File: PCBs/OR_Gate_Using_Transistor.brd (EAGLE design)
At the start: 28 x 26.8 mm, 11 parts, among them T1 BC547, T2 BC547

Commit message: Updated
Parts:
- moved OUTPUT 27.3 mm to (19.3, 31.6), turned to 180 degrees
- moved B 20.9 mm to (11.7, 31.6), turned to 180 degrees
- moved A 19.3 mm to (4.28, 31.7), turned to 180 degrees
- moved 5V 7.98 mm to (4.21, 7.09)
- moved GND 7.36 mm to (11.8, 7.05)
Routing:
- net 5V: track 33.3 -> 13.8 mm
- net N$7: track 5.23 -> 20.7 mm
- net N$6: track 6.89 -> 20.3 mm
- net N$3: track 30.9 -> 28.7 mm
- net GND: track 23.0 -> 23.5 mm
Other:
- board size 28 x 26.8 mm -> 29.8 x 38.8 mm
- board text added: "PinwheelRobotics"
- board text added: "care@pinwheel.in"

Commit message: New Update
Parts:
- moved OUTPUT 0.39 mm to (19.2, 32.0)
- moved B 0.38 mm to (11.8, 31.9)
- moved A 0.26 mm to (4.22, 31.9)
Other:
- board size 29.8 x 38.8 mm -> 29.5 x 39.1 mm
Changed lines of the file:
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@@
 <drawing>
 <settings>
-<setting alwaysvectorfont="yes"/>
+<setting alwaysvectorfont="no"/>
 <setting verticaltext="up"/>
 </settings>
@@
 <board>
 <plain>
-<wire x1="-3" y1="0" x2="26.8" y2="-0.061" width="0" layer="20"/>
-<wire x1="26.8" y1="-0.061" x2="26.8" y2="38.726" width="0" layer="20"/>
-<wire x1="26.8" y1="38.726" x2="-2.9" y2="38.66" width="0" layer="20"/>
-<wire x1="-2.9" y1="38.66" x2="-3" y2="0" width="0" layer="20"/>
-<hole x="-1" y="36.5" drill="3"/>
-<hole x="24.5" y="36.5" drill="3"/>
+<wire x1="-3" y1="38.198590625" x2="-3" y2="1.653915625" width="0" layer="20"/>
+<wire x1="-3" y1="1.653915625" x2="-1.3460875" y2="-0.00341875" width="0" layer="20" curve="89.881486"/>
+<wire x1="-1.3460875" y1="-0.00341875" x2="24.954165625" y2="-0.057803125" width="0" layer="20"/>
+<wire x1="24.954165625" y1="-0.057803125" x2="26.5" y2="1.4848375" width="0" layer="20" curve="90.106059"/>
+<wire x1="26.5" y1="1.4848375" x2="26.5" y2="37.990275" width="0" layer="20"/>
+<wire x1="26.5" y1="37.990275" x2="25.490275" y2="39" width="0" layer="20" curve="90"/>
+<wire x1="25.490275" y1="39" x2="-2.198590625" y2="39" width="0" layer="20"/>
+<wire x1="-2.198590625" y1="39" x2="-3" y2="38.198590625" width="0" layer="20" curve="90"/>
+<hole x="-1" y="37" drill="3"/>
+<hole x="24.5" y="37" drill="3"/>
 <hole x="-1" y="2" drill="3"/>
-<hole x="24.5" y="2.5" drill="3"/>
+<hole x="24.5" y="2" drill="3"/>
 <text x="0" y="10.5" size="1.778" layer="21" rot="R90">PinwheelRobotics</text>
-<text x="20" y="25.5" size="1.778" layer="22" rot="MR270">care@pinwheel.in</text>
+<text x="24.572" y="27.786" size="1.778" layer="22" rot="MR270">care@pinwheel.in</text>
 </plain>
 <attributes>
@@
 <attribute name="NAME" x="3.32" y="10.773" size="0.4064" layer="21" font="vector"/>
 </element>
-<element name="A" library="microbit" package="MICROBIT_PAD" value="MICROBIT_PAD" x="4.278" y="31.657" smashed="yes" rot="R180">
-<attribute name="NAME" x="4.913" y="28.101" size="1.27" layer="21" rot="R180"/>
-</element>
-<element name="B" library="microbit" package="MICROBIT_PAD" value="MICROBIT_PAD" x="11.746" y="31.554" smashed="yes" rot="R180">
-<attribute name="NAME" x="13.016" y="27.617" size="0.4064" layer="21" rot="R180"/>
+<element name="A" library="microbit" package="MICROBIT_PAD" value="MICROBIT_PAD" x="4.223" y="31.915" smashed="yes" rot="R180">
+<attribute name="NAME" x="4.858" y="28.359" size="1.27" layer="21" rot="R180"/>
+</element>
+<element name="B" library="microbit" package="MICROBIT_PAD" value="MICROBIT_PAD" x="11.811" y="31.931" smashed="yes" rot="R180">
+<attribute name="NAME" x="13.081" y="27.994" size="0.4064" layer="21" rot="R180"/>
 </element>
 <element name="GND" library="microbit" package="MICROBIT_PAD" value="MICROBIT_PAD" x="11.808" y="7.051" smashed="yes">
@@
 <attribute name="VALUE" x="12.7" y="21.971" size="1.27" layer="27" ratio="10"/>
 </element>
-<element name="OUTPUT" library="microbit" package="MICROBIT_PAD" value="MICROBIT_PAD" x="19.295" y="31.596" smashed="yes" rot="R180">
-<attribute name="NAME" x="15.993" y="28.167" size="0.3048" layer="21" font="vector"/>
+<element name="OUTPUT" library="microbit" package="MICROBIT_PAD" value="MICROBIT_PAD" x="19.226" y="31.981" smashed="yes" rot="R180">
+<attribute name="NAME" x="18.337" y="28.044" size="0.3048" layer="21" font="vector"/>
 </element>
 <element name="R1" library="we-rcl" package="R0207/7" value="" x="10.922" y="15.621" smashed="yes" rot="R180">
@@
 <wire x1="7.5" y1="19.5" x2="7.045" y2="19.05" width="0.254" layer="16"/>
 <wire x1="17.5" y1="31.5" x2="10" y2="24" width="0.254" layer="1"/>
-<wire x1="19" y1="31.5" x2="17.5" y2="31.5" width="0.254" layer="1"/>
+<wire x1="17.747928125" y1="31.5" x2="17.5" y2="31.5" width="0.254" layer="1"/>
 <wire x1="10" y1="24" x2="9.525" y2="23.622" width="0.254" layer="1"/>
-<wire x1="19" y1="31.5" x2="19.295" y2="31.596" width="0.254" layer="1"/>
+<wire x1="17.747928125" y1="31.5" x2="19.226" y2="31.981" width="0.254" layer="1"/>
 </signal>
 <signal name="GND">
@@
 <contactref element="R1" pad="1"/>
 <wire x1="4.5" y1="26" x2="14.5" y2="16" width="0.254" layer="1"/>
-<wire x1="4.5" y1="31.5" x2="4.5" y2="26" width="0.254" layer="1"/>
+<wire x1="4.5" y1="31.719103125" x2="4.5" y2="26" width="0.254" layer="1"/>
 <wire x1="14.5" y1="16" x2="14.672" y2="15.621" width="0.254" layer="1"/>
-<wire x1="4.5" y1="31.5" x2="4.278" y2="31.657" width="0.254" layer="1"/>
+<wire x1="4.5" y1="31.719103125" x2="4.223" y2="31.915" width="0.254" layer="1"/>
 </signal>
 <signal name="N$7">
@@
 <wire x1="13.5" y1="13.5" x2="14.5" y2="12.5" width="0.254" layer="16"/>
 <wire x1="13.5" y1="30" x2="13.5" y2="13.5" width="0.254" layer="16"/>
-<wire x1="12" y1="31.5" x2="13.5" y2="30" width="0.254" layer="16"/>
+<wire x1="11.876340625" y1="31.623659375" x2="13.5" y2="30" width="0.254" layer="16"/>
 <wire x1="14.5" y1="12.5" x2="14.545" y2="12.065" width="0.254" layer="16"/>
-<wire x1="12" y1="31.5" x2="11.746" y2="31.554" width="0.254" layer="16"/>
+<wire x1="11.876340625" y1="31.623659375" x2="11.811" y2="31.931" width="0.254" layer="16"/>
 </signal>
 </signals>

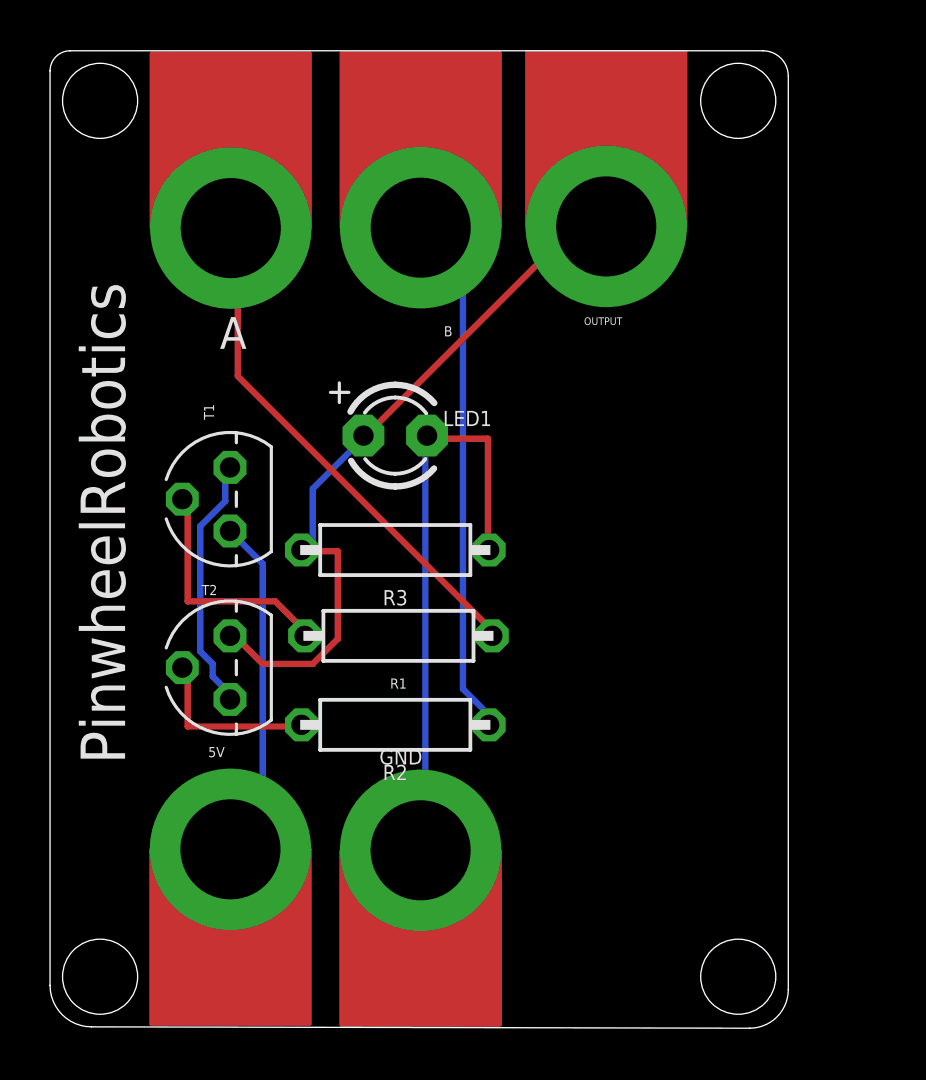
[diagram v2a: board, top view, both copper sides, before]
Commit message: New Update for board curv
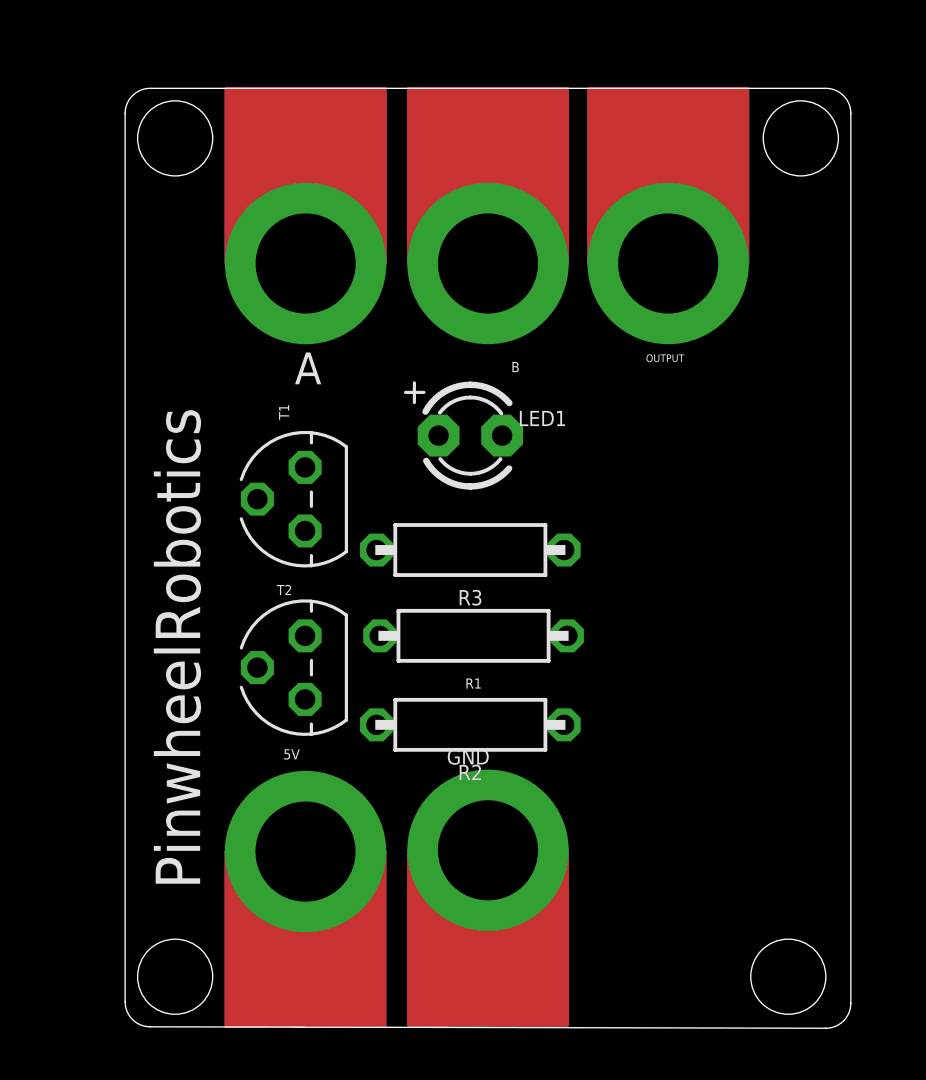
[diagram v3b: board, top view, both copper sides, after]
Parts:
- moved A 3.31 mm to (7.21, 30.5)
- moved B 3.05 mm to (14.5, 30.5)
- moved 5V 3.00 mm to (7.21, 7.00)
- moved LED1 3.00 mm to (13.8, 23.6)
- moved R1 3.00 mm to (13.9, 15.6)
- moved R2 3.00 mm to (13.8, 12.1)
- moved R3 3.00 mm to (13.8, 19.1)
- moved T1 3.00 mm to (7.19, 21.1)
- moved T2 3.00 mm to (7.19, 14.4)
- moved OUTPUT 2.88 mm to (21.7, 30.5)
- moved GND 2.69 mm to (14.5, 7.05)
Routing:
- net N$3: track 28.7 -> 0.00 mm
- net GND: track 23.5 -> 0.00 mm
- net N$7: track 21.0 -> 0.00 mm
- net N$6: track 20.6 -> 0.00 mm
- net 5V: track 13.8 -> 0.00 mm
- net N$2: track 10.2 -> 0.00 mm
- net N$4: track 9.56 -> 0.00 mm
- net N$1: track 6.99 -> 0.00 mm
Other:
- board size 29.5 x 39.1 mm -> 29 x 37.6 mm

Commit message: Dimension added
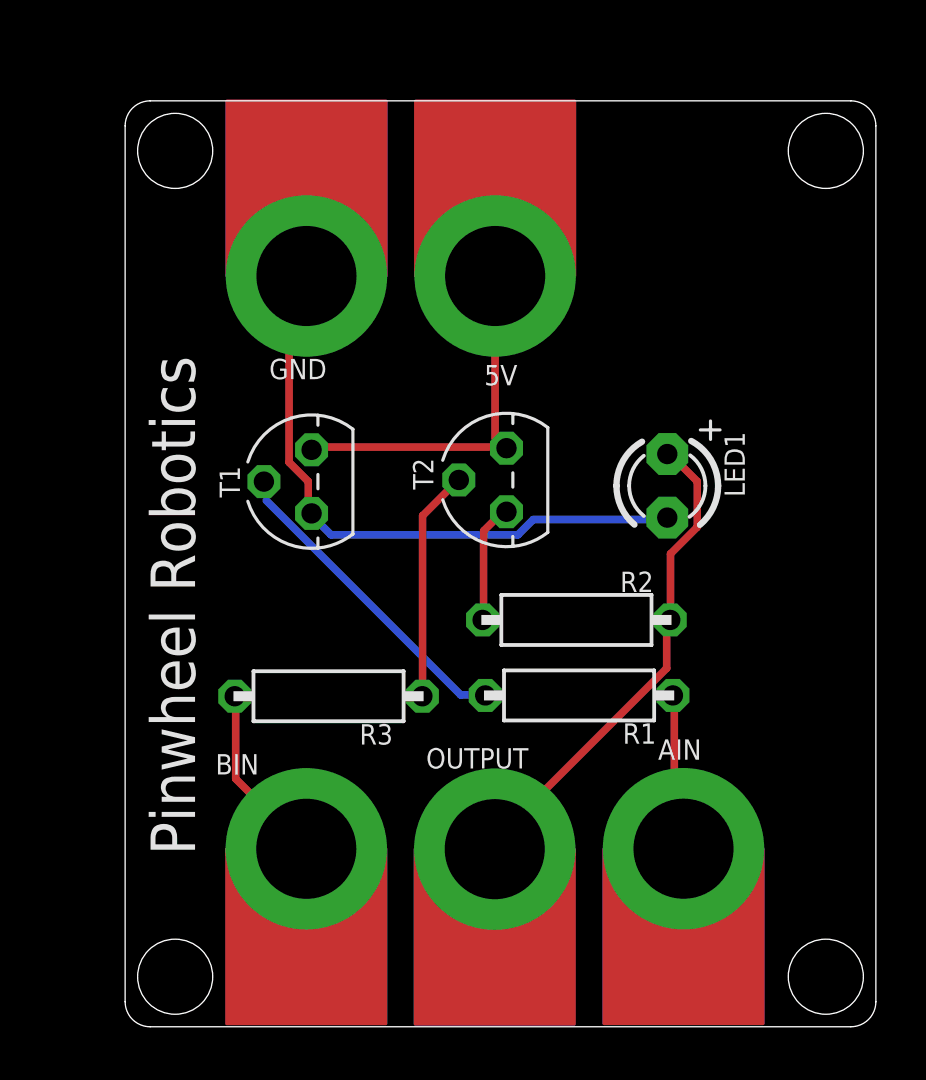
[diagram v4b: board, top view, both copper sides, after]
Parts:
- removed A, B: MICROBIT_PAD, microbit:MICROBIT_PAD
- added AIN, BIN: MICROBIT_PAD, microbit:MICROBIT_PAD
- R1, R3: value (none) -> 10k
- R2: value (none) -> 470
- T1, T2: value BC547 -> 2N3904; device transistor-neu-to92:TO92 -> transistor:TO92
- moved OUTPUT 24.4 mm to (14.8, 7.10), turned to 0 degrees
- moved 5V 24.2 mm to (14.8, 30.0), turned to 180 degrees
- moved GND 24.1 mm to (7.25, 30.0), turned to 180 degrees
- moved T2 11.0 mm to (15.2, 21.9)
- moved R3 8.14 mm to (8.13, 13.2)
- moved LED1 8.12 mm to (21.7, 21.6), turned to 270 degrees
- moved R2 5.96 mm to (18.0, 16.3)
- moved R1 4.84 mm to (18.1, 13.2)
- moved T1 0.75 mm to (7.45, 21.8)
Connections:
- removed net N$1: R2.2, T2.2
- new net N$5: AIN.PAD, R1.1
- net 5V: now also T1.1, T2.1; no longer T1.3
- net GND: now also T1.3; no longer R3.1
- net N$2: now also BIN.PAD, R3.2; no longer T1.1, T2.3
- net N$3: now also R3.1, T2.2; no longer LED1.A, OUTPUT.PAD, R3.2, T2.1
- net N$6: now also LED1.A, OUTPUT.PAD, R2.1; no longer A.PAD, R1.1
- net N$7: now also R2.2, T2.3; no longer B.PAD, R2.1
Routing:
- net GND: track 0.00 -> 25.0 mm
- net N$6: track 0.00 -> 19.7 mm
- net 5V: track 0.00 -> 15.2 mm
- net N$4: track 0.00 -> 12.8 mm
- net N$3: track 0.00 -> 9.25 mm
- net N$2: track 0.00 -> 7.28 mm
- net N$5: track 0.00 -> 6.29 mm
- net N$7: track 0.00 -> 4.80 mm
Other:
- board size 29 x 37.6 mm -> 30 x 37 mm
- board text added: "Pinwheel Robotics"
- board text removed: "PinwheelRobotics"
